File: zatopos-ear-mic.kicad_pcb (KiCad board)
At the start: 2 copper layers, 80 x 40 mm, 25 parts, among them J2 Conn_01x06_Socket, U1 NJU7043, U2 MCP3002

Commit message: Replace footprints
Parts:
- C1, C2, C5: footprint Capacitor_SMD:C_1206_3216Metric -> Capacitor_SMD:C_0603_1608Metric
- C3, C4: value 12p -> 100p; footprint Capacitor_SMD:C_1206_3216Metric -> Capacitor_SMD:C_0603_1608Metric
- R1, R2: footprint Resistor_SMD:R_1206_3216Metric -> Resistor_SMD:R_0603_1608Metric
- R3, R4: value 10k -> 1k; footprint Resistor_SMD:R_1206_3216Metric -> Resistor_SMD:R_0603_1608Metric
- R5, R6: value 1M -> 100k; footprint Resistor_SMD:R_1206_3216Metric -> Resistor_SMD:R_0603_1608Metric
- R7, R8: value 100k -> 10k; footprint Resistor_SMD:R_1206_3216Metric -> Resistor_SMD:R_0603_1608Metric
- RV1, RV2: value 0~500k -> 0~50k
- moved C5 2.69 mm to (158.0, 86.0)
- moved R4 2.24 mm to (142.0, 88.5)
- moved R8 2.24 mm to (158.0, 88.5)
- moved R3 1.80 mm to (158.0, 91.0)
- moved C4 1.12 mm to (142.0, 91.0)
- moved R5 1.12 mm to (158.0, 96.0)
- moved C3 1.00 mm to (158.0, 93.5)
- moved R6 1.00 mm to (142.0, 93.5)
- moved R1 0.71 mm to (174.0, 99.5)
- moved R2 0.71 mm to (126.0, 99.5)
- moved R7 0.71 mm to (145.0, 84.0)
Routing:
- net +3.3V: track 125.0 -> 128.4 mm
- net Net-(U1-B_IN-): track 19.1 -> 17.0 mm
- net Net-(C1-Pad1): track 4.89 -> 6.78 mm
- net Net-(R5-Pad1): track 4.57 -> 6.42 mm
- net Net-(R6-Pad2): track 10.8 -> 12.5 mm
- net Net-(U1-A_IN-): track 17.9 -> 16.2 mm
- net OFFSET: track 23.1 -> 21.7 mm
- net SOUND2: track 15.7 -> 14.7 mm
- net SOUND1: track 13.9 -> 12.9 mm
- net Net-(C2-Pad1): track 6.68 -> 7.64 mm
- net GND: track 9.64 -> 10.3 mm

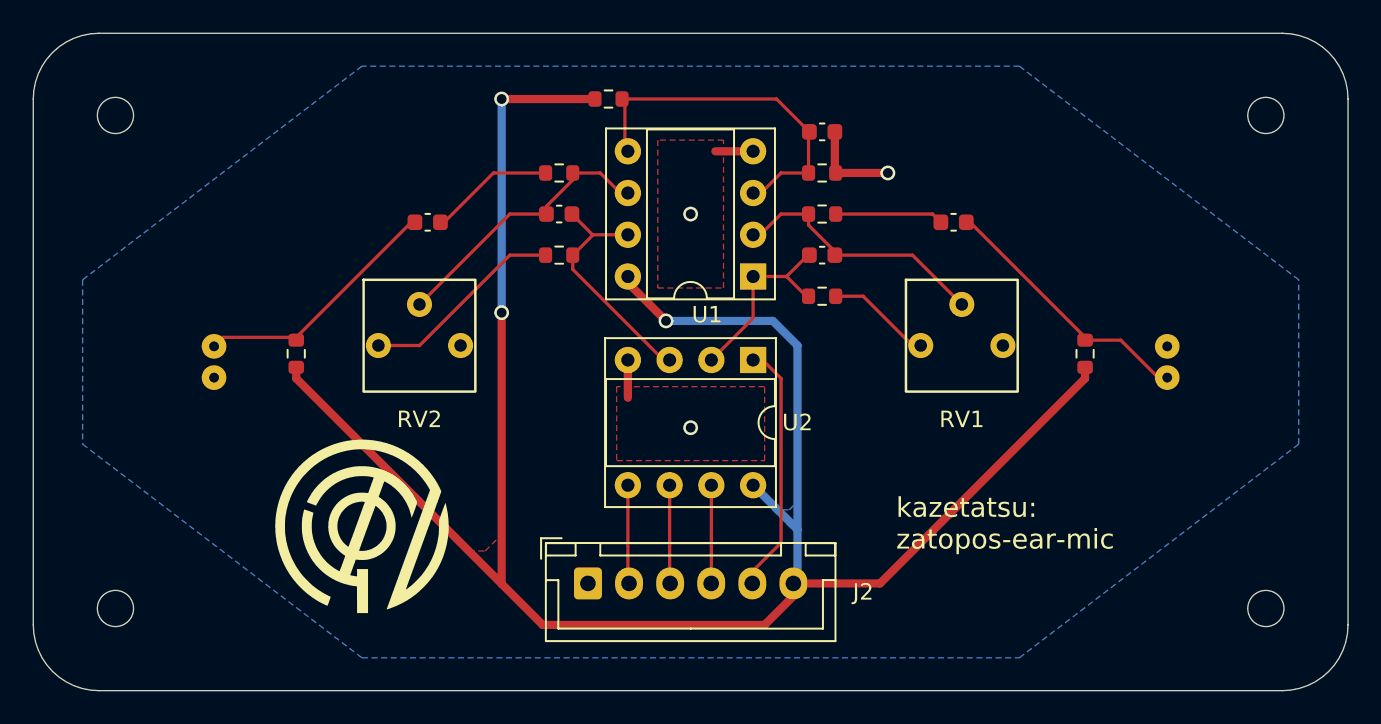
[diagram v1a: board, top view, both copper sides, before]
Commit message: Change place: OPamp and registers closer
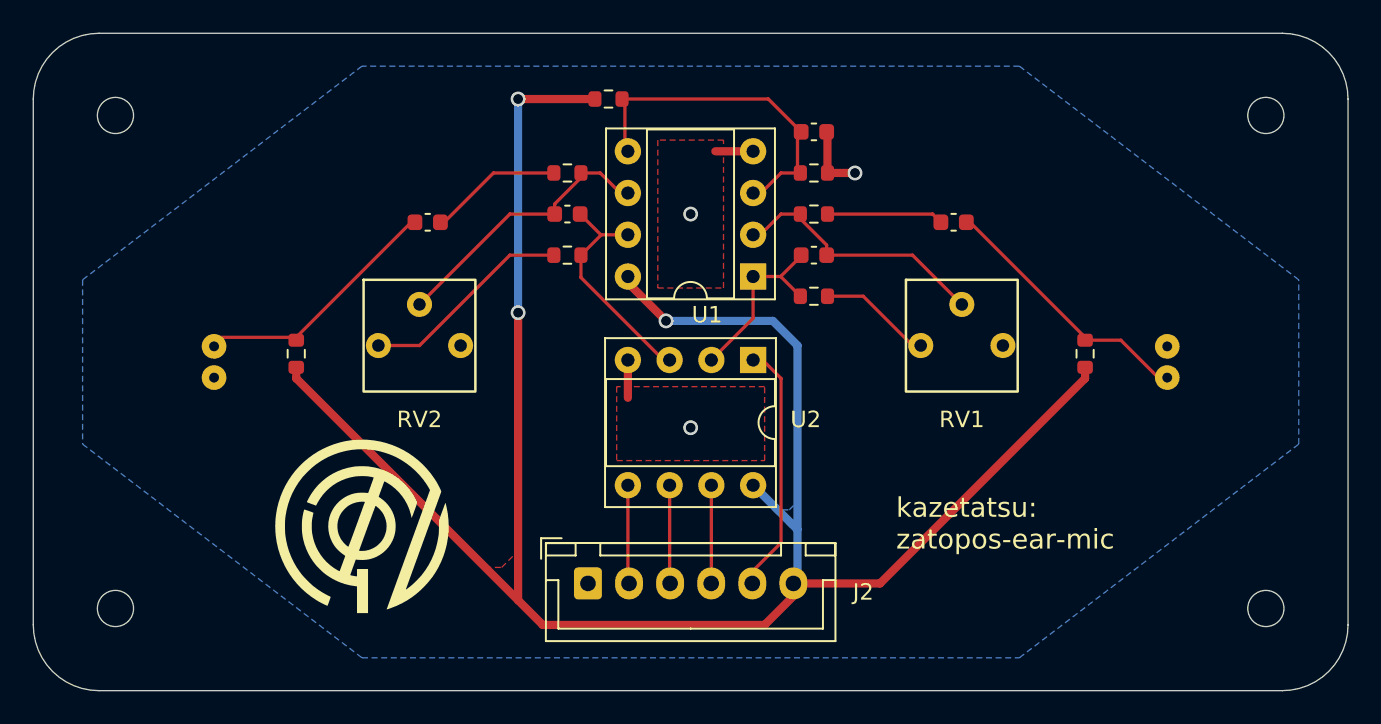
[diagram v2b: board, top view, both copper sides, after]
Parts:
- moved C3 0.50 mm to (157.5, 93.5)
- moved C4 0.50 mm to (142.5, 91.0)
- moved C5 0.50 mm to (157.5, 86.0)
- moved R3 0.50 mm to (157.5, 91.0)
- moved R4 0.50 mm to (142.5, 88.5)
- moved R5 0.50 mm to (157.5, 96.0)
- moved R6 0.50 mm to (142.5, 93.5)
- moved R8 0.50 mm to (157.5, 88.5)
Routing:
- net GND: track 10.3 -> 8.73 mm
- net OFFSET: track 21.7 -> 20.6 mm
- net SOUND2: track 14.7 -> 14.0 mm
- net SOUND1: track 12.9 -> 12.3 mm
- net Net-(R6-Pad2): track 12.5 -> 13.0 mm
- net Net-(R5-Pad1): track 6.42 -> 6.92 mm
- net Net-(C2-Pad1): track 7.64 -> 8.14 mm
